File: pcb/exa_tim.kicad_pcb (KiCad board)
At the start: 4 copper layers, 42 x 42 mm, 52 parts, among them J1 20021112-00010T4LF, J2 FH12-24S-0.5SH(55), Q1 SI2333DS-T1-E3, Q2 DMN3067LW-7, SW1 TL3305CF260QG, SW2 TL3305CF260QG, SW3 TL3305CF260QG, SW4 TL3305CF260QG, U1 STM32L071KZUx, U2 CAM-M8C-0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

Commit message: Changed 2x06 header to 2x05 header
I choosed the wrong header for the Cortex Debug header.
This is the correct header. The old header is working fine
but two holes are not used.
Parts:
- J1: footprint Connector_PinHeader_1.27mm:PinHeader_2x06_P1.27mm_Horizontal -> Connector_PinHeader_1.27mm:PinHeader_2x05_P1.27mm_Horizontal
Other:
- board text added: "DC 180914"
- board text removed: "DC 180831"
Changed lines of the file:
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@@
-(kicad_pcb (version 20171130) (host pcbnew "(5.0.0)")
+(kicad_pcb (version 20171130) (host pcbnew 5.0.0-fee4fd1~66~ubuntu18.04.1)
   (general
     (thickness 1)
@@
     (add_net /GNSS_VDD)
   )
-  (module Connector_PinHeader_1.27mm:PinHeader_2x06_P1.27mm_Horizontal (layer F.Cu)
+  (module Connector_PinHeader_1.27mm:PinHeader_2x05_P1.27mm_Horizontal (layer F.Cu)
     (at 134.7 88.2)
-    (descr "Through hole angled pin header, 2x06, 1.27mm pitch, 4.0mm pin length, double rows")
-    (tags "Through hole angled pin header THT 2x06 1.27mm double row")
+    (descr "Through hole angled pin header, 2x05, 1.27mm pitch, 4.0mm pin length, double rows")
+    (tags "Through hole angled pin header THT 2x05 1.27mm double row")
     (fp_text reference J1 (at 3.0675 -1.635) (layer F.SilkS)
       (effects (font (size 1 1) (thickness 0.15)))
     )
-    (fp_text value 20021112-00010T4LF (at 3.0675 7.985) (layer F.Fab)
+    (fp_text value 20021112-00010T4LF (at 3.0675 6.715) (layer F.Fab)
       (effects (font (size 1 1) (thickness 0.15)))
     )
     (fp_line (start 2.02 -0.635) (end 2.77 -0.635) (layer F.Fab) (width 0.1))
-    (fp_line (start 2.77 -0.635) (end 2.77 6.985) (layer F.Fab) (width 0.1))
-    (fp_line (start 2.77 6.985) (end 1.77 6.985) (layer F.Fab) (width 0.1))
-    (fp_line (start 1.77 6.985) (end 1.77 -0.385) (layer F.Fab) (width 0.1))
+    (fp_line (start 2.77 -0.635) (end 2.77 5.715) (layer F.Fab) (width 0.1))
+    (fp_line (start 2.77 5.715) (end 1.77 5.715) (layer F.Fab) (width 0.1))
+    (fp_line (start 1.77 5.715) (end 1.77 -0.385) (layer F.Fab) (width 0.1))
     (fp_line (start 1.77 -0.385) (end 2.02 -0.635) (layer F.Fab) (width 0.1))
     (fp_line (start -0.2 -0.2) (end 1.77 -0.2) (layer F.Fab) (width 0.1))
@@
     (fp_line (start 6.77 4.88) (end 6.77 5.28) (layer F.Fab) (width 0.1))
     (fp_line (start 2.77 5.28) (end 6.77 5.28) (layer F.Fab) (width 0.1))
-    (fp_line (start -0.2 6.15) (end 1.77 6.15) (layer F.Fab) (width 0.1))
-    (fp_line (start -0.2 6.15) (end -0.2 6.55) (layer F.Fab) (width 0.1))
-    (fp_line (start -0.2 6.55) (end 1.77 6.55) (layer F.Fab) (width 0.1))
-    (fp_line (start 2.77 6.15) (end 6.77 6.15) (layer F.Fab) (width 0.1))
-    (fp_line (start 6.77 6.15) (end 6.77 6.55) (layer F.Fab) (width 0.1))
-    (fp_line (start 2.77 6.55) (end 6.77 6.55) (layer F.Fab) (width 0.1))
     (fp_line (start 1.71 -0.619677) (end 1.71 -0.695) (layer F.SilkS) (width 0.12))
     (fp_line (start 1.71 -0.695) (end 2.83 -0.695) (layer F.SilkS) (width 0.12))
-    (fp_line (start 2.83 -0.695) (end 2.83 7.045) (layer F.SilkS) (width 0.12))
-    (fp_line (start 2.83 7.045) (end 1.71 7.045) (layer F.SilkS) (width 0.12))
-    (fp_line (start 1.71 7.045) (end 1.71 6.969677) (layer F.SilkS) (width 0.12))
+    (fp_line (start 2.83 -0.695) (end 2.83 5.775) (layer F.SilkS) (width 0.12))
+    (fp_line (start 2.83 5.775) (end 1.71 5.775) (layer F.SilkS) (width 0.12))
+    (fp_line (start 1.71 5.775) (end 1.71 5.699677) (layer F.SilkS) (width 0.12))
     (fp_line (start 2.83 -0.26) (end 6.83 -0.26) (layer F.SilkS) (width 0.12))
     (fp_line (start 6.83 -0.26) (end 6.83 0.26) (layer F.SilkS) (width 0.12))
@@
     (fp_line (start 6.83 4.82) (end 6.83 5.34) (layer F.SilkS) (width 0.12))
     (fp_line (start 6.83 5.34) (end 2.83 5.34) (layer F.SilkS) (width 0.12))
-    (fp_line (start 1.71 5.715) (end 2.83 5.715) (layer F.SilkS) (width 0.12))
-    (fp_line (start 1.71 5.699677) (end 1.71 5.730323) (layer F.SilkS) (width 0.12))
-    (fp_line (start 2.83 6.09) (end 6.83 6.09) (layer F.SilkS) (width 0.12))
-    (fp_line (start 6.83 6.09) (end 6.83 6.61) (layer F.SilkS) (width 0.12))
-    (fp_line (start 6.83 6.61) (end 2.83 6.61) (layer F.SilkS) (width 0.12))
     (fp_line (start -0.76 0) (end -0.76 -0.76) (layer F.SilkS) (width 0.12))
     (fp_line (start -0.76 -0.76) (end 0 -0.76) (layer F.SilkS) (width 0.12))
-    (fp_line (start -1.15 -1.15) (end -1.15 7.5) (layer F.CrtYd) (width 0.05))
-    (fp_line (start -1.15 7.5) (end 7.3 7.5) (layer F.CrtYd) (width 0.05))
-    (fp_line (start 7.3 7.5) (end 7.3 -1.15) (layer F.CrtYd) (width 0.05))
+    (fp_line (start -1.15 -1.15) (end -1.15 6.25) (layer F.CrtYd) (width 0.05))
+    (fp_line (start -1.15 6.25) (end 7.3 6.25) (layer F.CrtYd) (width 0.05))
+    (fp_line (start 7.3 6.25) (end 7.3 -1.15) (layer F.CrtYd) (width 0.05))
     (fp_line (start 7.3 -1.15) (end -1.15 -1.15) (layer F.CrtYd) (width 0.05))
-    (fp_text user %R (at 2.27 3.175 90) (layer F.Fab)
+    (fp_text user %R (at 2.27 2.54 90) (layer F.Fab)
       (effects (font (size 0.6 0.6) (thickness 0.09)))
     )
@@
     (pad 10 thru_hole oval (at 1.27 5.08) (size 1 1) (drill 0.65) (layers *.Cu *.Mask)
       (net 51 /NRST))
-    (pad 11 thru_hole oval (at 0 6.35) (size 1 1) (drill 0.65) (layers *.Cu *.Mask))
-    (pad 12 thru_hole oval (at 1.27 6.35) (size 1 1) (drill 0.65) (layers *.Cu *.Mask))
-    (model ${KISYS3DMOD}/Connector_PinHeader_1.27mm.3dshapes/PinHeader_2x06_P1.27mm_Horizontal.wrl
+    (model ${KISYS3DMOD}/Connector_PinHeader_1.27mm.3dshapes/PinHeader_2x05_P1.27mm_Horizontal.wrl
       (at (xyz 0 0 0))
       (scale (xyz 1 1 1))
@@
     (effects (font (size 1 1) (thickness 0.15)))
   )
-  (gr_text "DC 180831" (at 132.3 73.6) (layer F.SilkS)
+  (gr_text "DC 180914" (at 132.3 73.6) (layer F.SilkS)
     (effects (font (size 1 1) (thickness 0.15)))
   )

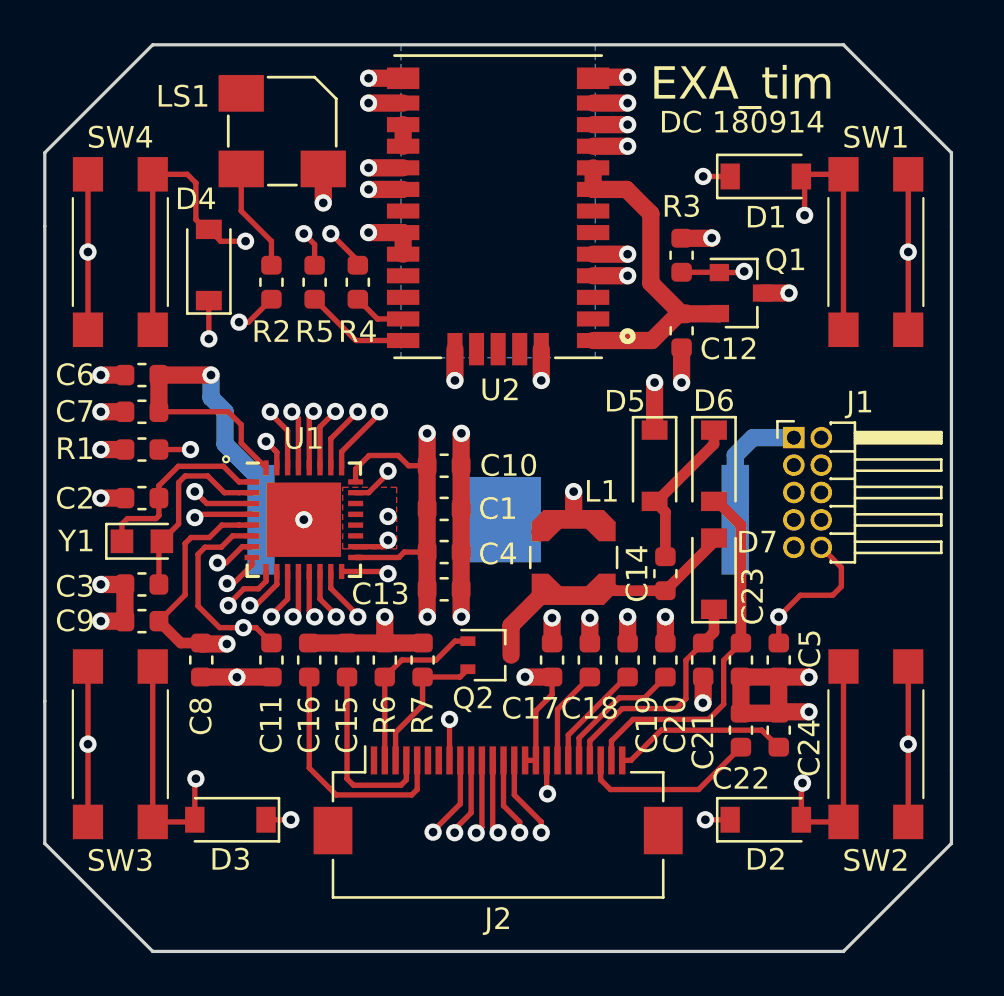
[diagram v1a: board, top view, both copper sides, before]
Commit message: Fix p-channel MOSFET and new routing
Fixed the p-channel MOSFET drain/source problem (was reversed).
New placement for the SWO header (2x05) for easier placement.
Re-routed signals, so that ground and power lane are signal trace
free.
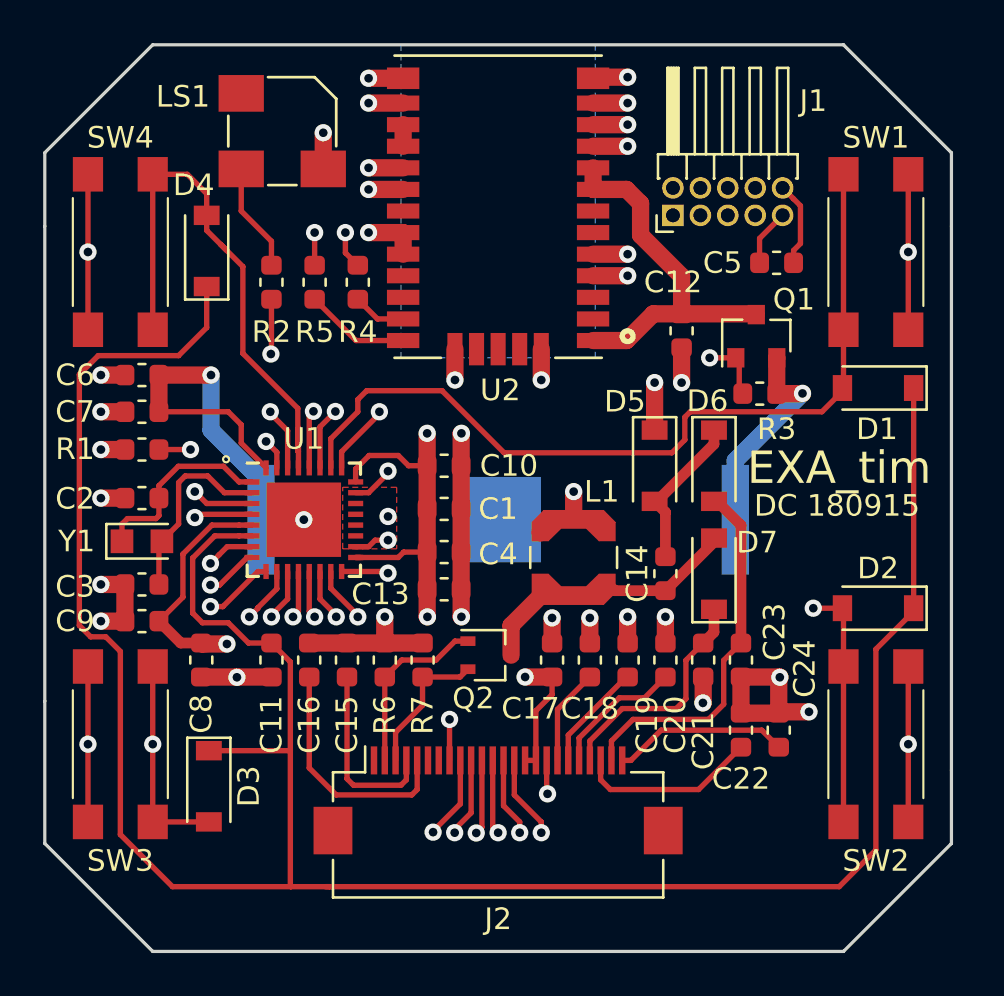
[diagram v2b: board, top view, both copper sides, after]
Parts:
- moved C5 18.4 mm to (133.9, 80.1), turned to 0 degrees
- moved J1 11.7 mm to (129.1, 77.9), turned to 90 degrees
- moved D1 11.1 mm to (138.6, 85.9), turned to 180 degrees
- moved D2 11.1 mm to (138.6, 96.1), turned to 180 degrees
- moved R3 7.36 mm to (133.1, 86.2), turned to 0 degrees
- moved Q1 2.12 mm to (133.0, 83.5), turned to 90 degrees
- moved D3 1.84 mm to (107.6, 104.3), turned to 270 degrees
- moved D4 0.66 mm to (107.5, 79.5)
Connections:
- Q1 pad 2: /GNSS_VDD -> 3V
- Q1 pad 3: 3V -> /GNSS_VDD
- R3 pad 1: 3V -> /GNSS_EN
- R3 pad 2: /GNSS_EN -> 3V
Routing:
- net /GNSS_EN: track 35.2 -> 64.6 mm
- net /BTN2: track 49.7 -> 42.6 mm
- net /NRST: track 39.2 -> 45.7 mm, vias 2 -> 1
- net /BTN3: track 35.9 -> 31.0 mm
- net /GNSS_VDD: track 15.8 -> 17.5 mm
- net GND: track 85.6 -> 86.9 mm
- net /ALARM: track 18.5 -> 17.4 mm
- net 3V: track 95.7 -> 96.8 mm, vias 12 -> 11
- net /TX: track 25.8 -> 24.7 mm
- net /RX: track 31.2 -> 30.4 mm
- net /SWCLK: track 27.1 -> 27.9 mm
- net /BTN4: track 25.3 -> 26.0 mm, vias 2 -> 0
- net /WKUP1: track 115.1 -> 115.6 mm, vias 5 -> 0
- net /BTN1: track 40.1 -> 40.0 mm, vias 2 -> 0
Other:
- board text added: "DC 180915"
- board text removed: "DC 180914"

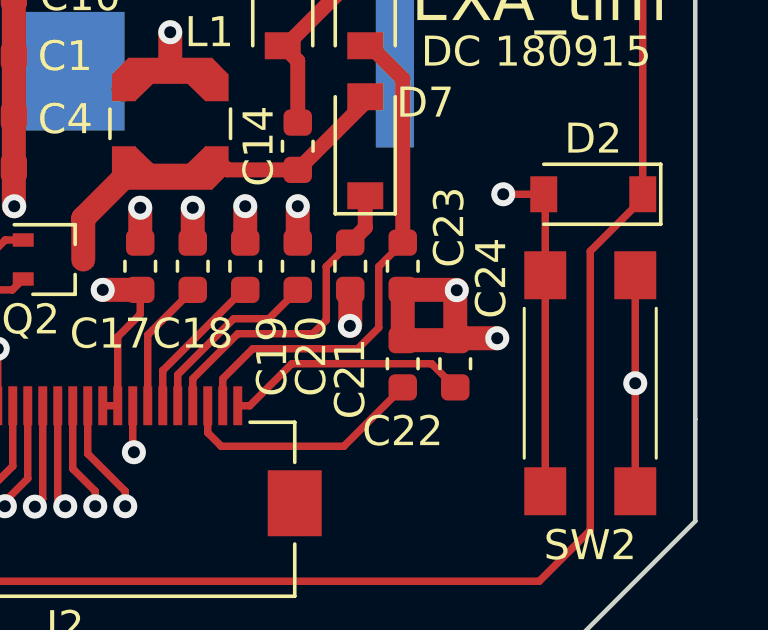
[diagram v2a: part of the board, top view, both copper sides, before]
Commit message: Reroute some GND vias
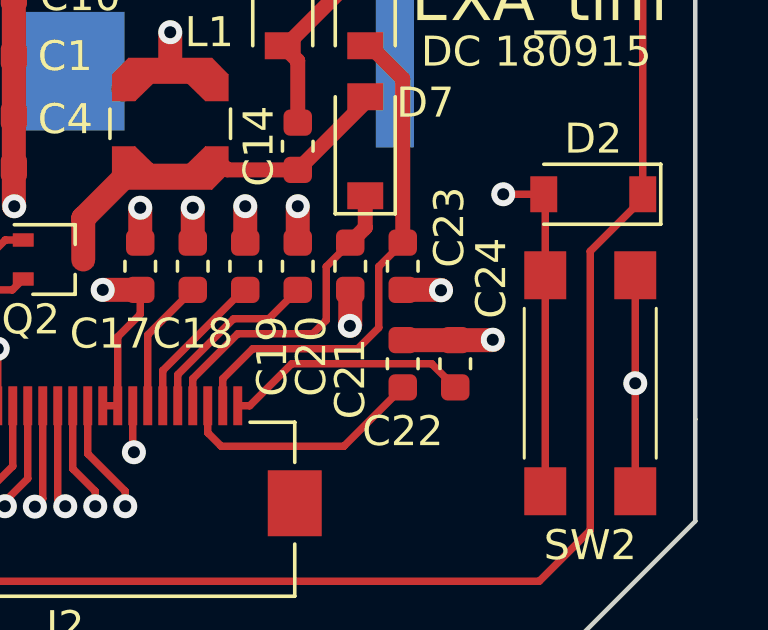
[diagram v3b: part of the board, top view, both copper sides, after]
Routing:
- net GND: track 86.9 -> 83.0 mm
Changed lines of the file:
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@@
     (thickness 1)
     (drawings 27)
-    (tracks 604)
+    (tracks 603)
     (zones 0)
     (modules 52)
@@
   (via (at 127 79.7) (size 0.8) (drill 0.4) (layers F.Cu B.Cu) (net 2))
   (segment (start 130.48734 99.30016) (end 130.5 99.2875) (width 0.25) (layer F.Cu) (net 2) (status 30))
-  (via (at 134.05 99.3) (size 0.8) (drill 0.4) (layers F.Cu B.Cu) (net 2))
-  (via (at 135.4 100.9) (size 0.8) (drill 0.4) (layers F.Cu B.Cu) (net 2))
-  (segment (start 135.3375 100.9625) (end 135.4 100.9) (width 0.25) (layer F.Cu) (net 2))
   (via (at 125.25 96.55) (size 0.8) (drill 0.4) (layers F.Cu B.Cu) (net 2))
   (via (at 123.5 96.550002) (size 0.8) (drill 0.4) (layers F.Cu B.Cu) (net 2))
@@
   (via (at 127 74.7) (size 0.8) (drill 0.4) (layers F.Cu B.Cu) (net 2))
   (segment (start 125.4 74.7) (end 127 74.7) (width 0.8) (layer F.Cu) (net 2) (status 10))
-  (segment (start 134.0625 100.9) (end 134 100.9625) (width 0.8) (layer F.Cu) (net 2) (status 30))
-  (segment (start 135.4 100.9) (end 134.0625 100.9) (width 0.8) (layer F.Cu) (net 2) (status 20))
   (segment (start 134 100.9625) (end 132.25 100.9625) (width 0.8) (layer F.Cu) (net 2) (status 30))
-  (segment (start 132.25 100.9625) (end 132.25 99.2875) (width 0.8) (layer F.Cu) (net 2) (status 30))
   (segment (start 130.5 100.47468) (end 130.48734 100.48734) (width 0.8) (layer F.Cu) (net 2))
   (segment (start 130.5 99.2875) (end 130.5 100.47468) (width 0.8) (layer F.Cu) (net 2) (status 10))
@@
   (via (at 129.5 85.65) (size 0.8) (drill 0.4) (layers F.Cu B.Cu) (net 2))
   (segment (start 129.5 85.65) (end 129.5 84.0375) (width 0.8) (layer F.Cu) (net 2) (status 20))
-  (segment (start 134.0375 99.2875) (end 134.05 99.3) (width 0.8) (layer F.Cu) (net 2))
-  (segment (start 132.25 99.2875) (end 134.0375 99.2875) (width 0.8) (layer F.Cu) (net 2) (status 10))
-  (segment (start 134 99.35) (end 134.05 99.3) (width 0.8) (layer F.Cu) (net 2))
-  (segment (start 134 100.9625) (end 134 99.35) (width 0.8) (layer F.Cu) (net 2) (status 10))
   (segment (start 133.1125 78.9675) (end 134.18 77.9) (width 0.25) (layer F.Cu) (net 2) (status 20))
   (segment (start 133.1125 80.1) (end 133.1125 78.9675) (width 0.25) (layer F.Cu) (net 2) (status 10))
@@
   (via (at 115.899996 94.47501) (size 0.8) (drill 0.4) (layers F.Cu B.Cu) (net 2))
   (segment (start 112.9 74.075) (end 112.9 75.75) (width 0.8) (layer F.Cu) (net 2))
+  (via (at 133.525 99.3) (size 0.8) (drill 0.4) (layers F.Cu B.Cu) (net 2))
+  (segment (start 132.25 99.2875) (end 133.5125 99.2875) (width 0.8) (layer F.Cu) (net 2))
+  (segment (start 133.5125 99.2875) (end 133.525 99.3) (width 0.8) (layer F.Cu) (net 2))
+  (segment (start 135.3375 100.9625) (end 135.4 100.9) (width 0.25) (layer F.Cu) (net 2))
+  (via (at 135.25 100.95) (size 0.8) (drill 0.4) (layers F.Cu B.Cu) (net 2))
+  (segment (start 135.3 100.9) (end 135.25 100.95) (width 0.25) (layer F.Cu) (net 2))
+  (segment (start 134 100.9625) (end 135.2375 100.9625) (width 0.8) (layer F.Cu) (net 2))
+  (segment (start 135.2375 100.9625) (end 135.25 100.95) (width 0.8) (layer F.Cu) (net 2))
+  (segment (start 135.4 100.9) (end 135.3 100.9) (width 0.25) (layer F.Cu) (net 2))
   (segment (start 117.5 100.6) (end 117.5 99.2875) (width 0.25) (layer F.Cu) (net 3) (status 20))
   (segment (start 116.25 103.15) (end 116.25 101.85) (width 0.25) (layer F.Cu) (net 3) (status 10))

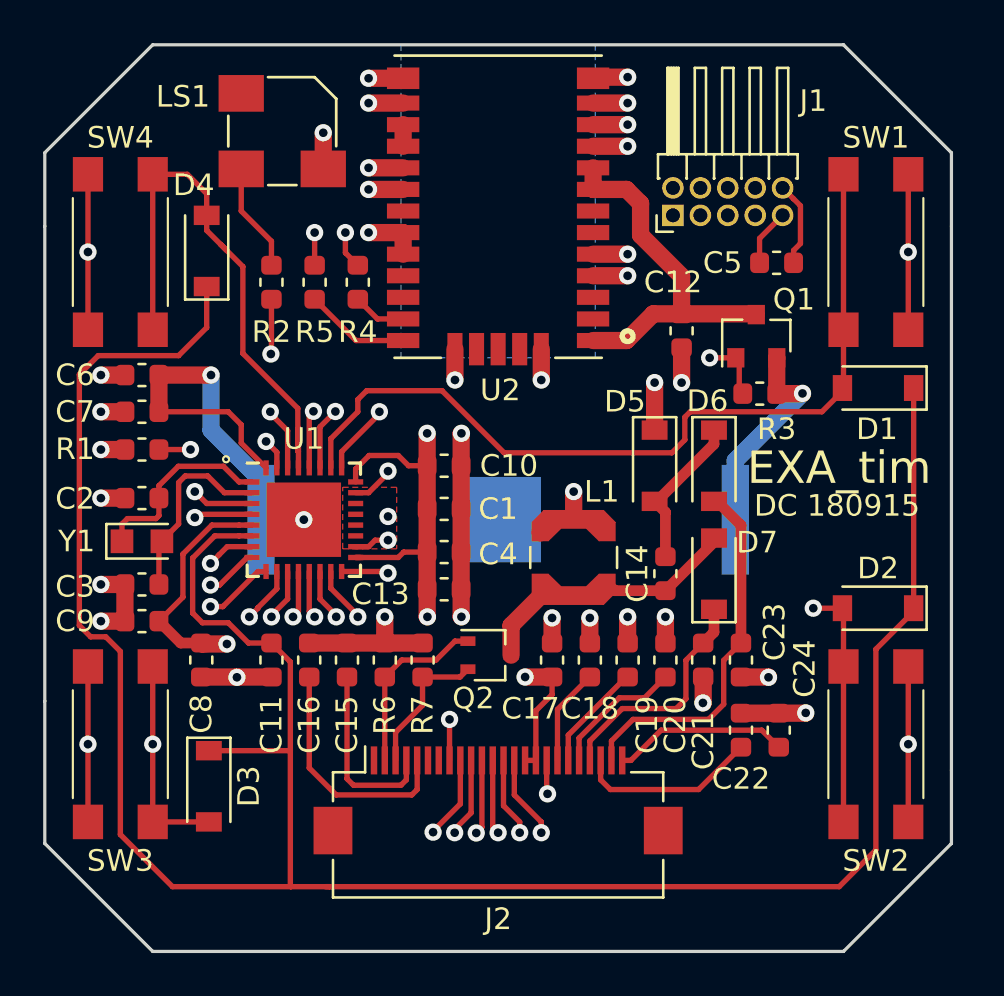
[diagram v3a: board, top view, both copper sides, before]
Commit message: Move epaper display connector more upward
This is needed, since the flexible connector hangs out too
much and wouldn't fit into the case otherwise.
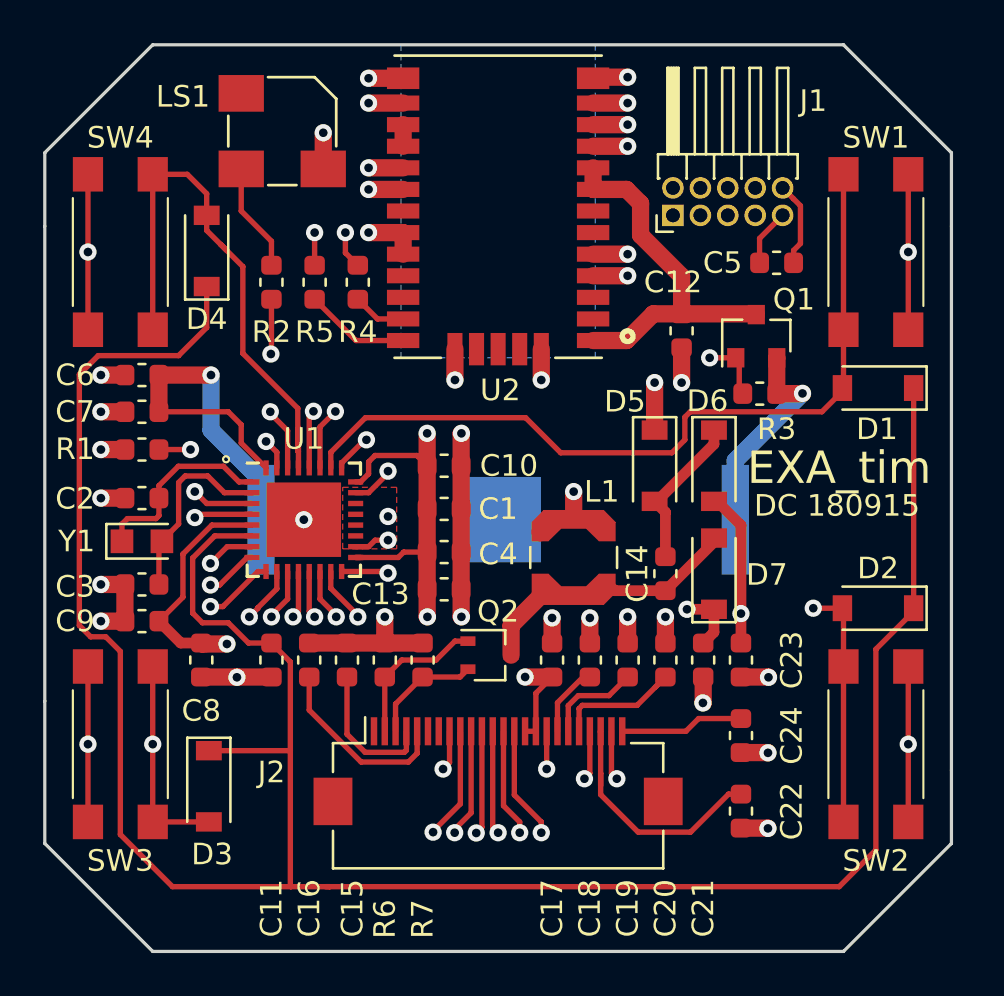
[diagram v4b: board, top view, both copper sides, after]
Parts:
- moved C22 3.75 mm to (132.2, 105.5), turned to 270 degrees
- moved C24 1.77 mm to (132.2, 102.0), turned to 270 degrees
- moved J2 1.35 mm to (121.0, 103.7)
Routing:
- net /PREVGH: track 10.8 -> 15.7 mm, vias 0 -> 2
- net /PREVGL: track 17.1 -> 20.5 mm, vias 0 -> 2
- net Net-(C22-Pad1): track 8.40 -> 11.5 mm
- net Net-(C16-Pad2): track 11.2 -> 8.72 mm
- net Net-(C24-Pad1): track 8.16 -> 5.74 mm
- net Net-(C15-Pad1): track 8.59 -> 6.67 mm
- net /BTN1: track 40.0 -> 38.3 mm
- net 3V: track 96.8 -> 95.4 mm
- net /SCK: track 31.6 -> 33.0 mm
- net /RESET: track 20.1 -> 21.4 mm
- net /RESE: track 6.63 -> 5.28 mm
- net /MOSI: track 26.5 -> 27.8 mm
- net /DC: track 22.1 -> 23.5 mm
- net /CS: track 21.5 -> 22.8 mm
- net /BUSY: track 23.2 -> 24.6 mm
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
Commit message: Add new font, add alarm, removed alarm series resistor
The series resistor was not needed, since the alarm would be too
tiny. I also added basic "beep" functionality.

Also added a new font face size 96.
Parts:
- removed the R2 at (110.5, 81.0)
- removed the R4 at (114.5, 81.0)
- added R3: 220, Resistor_SMD:R_0603_1608Metric, F.Cu at (114.0, 81.0)
- moved R4 0.75 mm to (111.8, 81.0)
- renumbered R3 to R2, R5 to R4, R6 to R5, R7 to R6
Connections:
- LS1 pad 1: Net-(LS1-Pad1) -> /ALARM
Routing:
- net /ALARM: track 17.4 -> 23.5 mm
- net Net-(LS1-Pad1): track 5.04 -> 0.00 mm
- net /RX_GNSS: track 4.89 -> 5.64 mm
- net /TX_GNSS: track 2.48 -> 2.98 mm
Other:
- board text added: "DC 180916"
- board text removed: "DC 180915"
